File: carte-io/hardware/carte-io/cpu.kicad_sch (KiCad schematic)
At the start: 24 parts, among them J3 FTSH-105-01-L-DV-007, SW1 SW_Push, SW2 SW_Push, U1 STM32U545VETx, X1 ASE-16.000MHZ-LC-T

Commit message: Carte version 1.1 terminée
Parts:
- J3: value FTSH-105-01-L-DV-007 -> FTSH-105-01-L-DH; footprint FTSH-105-01-L-DV-007-K:SAMTEC_FTSH-105-X-X-DV-007-P-X -> FTSH-105-01-L-DH:SAMTEC_FTSH-105-01-L-DH
- R28: value 1K -> 270R
- SW1, SW2: footprint Button_Switch_THT:SW_TH_Tactile_Omron_B3F-10xx -> Button_Switch_SMD:Panasonic_EVQPUJ_EVQPUA
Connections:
- net GEN_PWM1: no longer names the net of U1.67 (PA8)
- net GEN_PWM2: no longer names the net of U1.47 (PB10)
- net INPUT1 renamed IO1
- net INPUT2 renamed IO2
- net INPUT3 renamed IO3
- net INPUT4 renamed IO4
- net OUTPUT1: no longer names the net of U1.42 (PE11)
- net OUTPUT2 renamed ADC_AN1
- net OUTPUT3: no longer names the net of U1.45 (PE14)
- net OUTPUT4: no longer names the net of U1.46 (PE15)
- net SPI_CS: no longer names the net of U1.97 (PE0)
- net SPI_MISO: no longer names the net of U1.31 (PA6)
- net SPI_MOSI: no longer names the net of U1.32 (PA7)
- net SPI_SCK renamed ADC_AN2
- no-connect marks 18 -> 26
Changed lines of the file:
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@@
 	(title_block
 		(title "CPU")
-		(date "2024-10-09")
-		(rev "1.0")
+		(date "2025-02-25")
+		(rev "1.1")
 	)
 	(junction
@@
 	)
 	(no_connect
+		(at 104.14 58.42)
+	)
+	(no_connect
+		(at 149.86 104.14)
+	)
+	(no_connect
+		(at 104.14 86.36)
+	)
+	(no_connect
 		(at 149.86 114.3)
 	)
@@
 	)
 	(no_connect
+		(at 149.86 53.34)
+	)
+	(no_connect
 		(at 149.86 154.94)
 	)
@@
 	)
 	(no_connect
+		(at 149.86 50.8)
+	)
+	(no_connect
 		(at 104.14 60.96)
 	)
 	(no_connect
+		(at 149.86 55.88)
+	)
+	(no_connect
 		(at 149.86 73.66)
 	)
 	(no_connect
+		(at 104.14 96.52)
+	)
+	(no_connect
 		(at 149.86 157.48)
 	)
@@
 	)
 	(no_connect
+		(at 104.14 93.98)
+	)
+	(no_connect
 		(at 104.14 137.16)
 	)
@@
 	(wire
 		(pts
-			(xy 91.44 91.44) (xy 104.14 91.44)
+			(xy 50.8 187.96) (xy 58.42 187.96)
 		)
 		(stroke
@@
 	(wire
 		(pts
-			(xy 50.8 187.96) (xy 58.42 187.96)
+			(xy 91.44 88.9) (xy 104.14 88.9)
 		)
 		(stroke
@@
 	(wire
 		(pts
-			(xy 149.86 104.14) (xy 163.83 104.14)
-		)
-		(stroke
-			(width 0)
-			(type default)
-		)
-	)
-	(wire
-		(pts
 			(xy 91.44 124.46) (xy 104.14 124.46)
 		)
@@
 	(wire
 		(pts
-			(xy 91.44 86.36) (xy 104.14 86.36)
-		)
-		(stroke
-			(width 0)
-			(type default)
-		)
-	)
-	(wire
-		(pts
 			(xy 58.42 187.96) (xy 58.42 189.23)
 		)
@@
 	(wire
 		(pts
-			(xy 91.44 93.98) (xy 104.14 93.98)
+			(xy 91.44 91.44) (xy 104.14 91.44)
 		)
 		(stroke
@@
 	(wire
 		(pts
-			(xy 91.44 88.9) (xy 104.14 88.9)
-		)
-		(stroke
-			(width 0)
-			(type default)
-		)
-	)
-	(wire
-		(pts
 			(xy 25.4 130.81) (xy 25.4 128.27)
 		)
@@
 	(wire
 		(pts
-			(xy 149.86 50.8) (xy 163.83 50.8)
-		)
-		(stroke
-			(width 0)
-			(type default)
-		)
-	)
-	(wire
-		(pts
-			(xy 91.44 96.52) (xy 104.14 96.52)
-		)
-		(stroke
-			(width 0)
-			(type default)
-		)
-	)
-	(wire
-		(pts
 			(xy 76.2 43.18) (xy 90.17 43.18)
 		)
@@
 	(wire
 		(pts
-			(xy 96.52 58.42) (xy 104.14 58.42)
-		)
-		(stroke
-			(width 0)
-			(type default)
-		)
-	)
-	(wire
-		(pts
 			(xy 149.86 71.12) (xy 163.83 71.12)
 		)
@@
 	(wire
 		(pts
-			(xy 149.86 55.88) (xy 163.83 55.88)
-		)
-		(stroke
-			(width 0)
-			(type default)
-		)
-	)
-	(wire
-		(pts
 			(xy 44.45 55.88) (xy 44.45 58.42)
 		)
@@
 	(wire
 		(pts
-			(xy 149.86 53.34) (xy 163.83 53.34)
-		)
-		(stroke
-			(width 0)
-			(type default)
-		)
-	)
-	(wire
-		(pts
 			(xy 90.17 33.02) (xy 100.33 33.02)
 		)
@@
 		)
 	)
-	(hierarchical_label "OUTPUT2"
-		(shape output)
-		(at 91.44 88.9 180)
-		(effects
-			(font
-				(size 1.27 1.27)
-			)
-			(justify right)
-		)
-	)
-	(hierarchical_label "GEN_PWM1"
-		(shape output)
-		(at 163.83 55.88 0)
-		(effects
-			(font
-				(size 1.27 1.27)
-			)
-			(justify left)
-		)
-	)
 	(hierarchical_label "US_PulseStart"
 		(shape output)
@@
 		)
 	)
-	(hierarchical_label "OUTPUT3"
-		(shape output)
-		(at 91.44 93.98 180)
-		(effects
-			(font
-				(size 1.27 1.27)
-			)
-			(justify right)
-		)
-	)
 	(hierarchical_label "COM_USB_RX"
 		(shape input)
@@
 		)
 	)
-	(hierarchical_label "SPI_SCK"
-		(shape output)
-		(at 91.44 91.44 180)
-		(effects
-			(font
-				(size 1.27 1.27)
-			)
-			(justify right)
-		)
-	)
-	(hierarchical_label "SPI_MOSI"
-		(shape output)
-		(at 163.83 53.34 0)
-		(effects
-			(font
-				(size 1.27 1.27)
-			)
-			(justify left)
-		)
-	)
-	(hierarchical_label "OUTPUT1"
-		(shape output)
-		(at 91.44 86.36 180)
+	(hierarchical_label "ADC_AN1"
+		(shape input)
+		(at 91.44 88.9 180)
 		(effects
 			(font
@@
 		)
 	)
-	(hierarchical_label "GEN_PWM2"
-		(shape output)
-		(at 163.83 104.14 0)
-		(effects
-			(font
-				(size 1.27 1.27)
-			)
-			(justify left)
-		)
-	)
 	(hierarchical_label "INT_MAGNETO"
 		(shape input)
@@
 		)
 	)
-	(hierarchical_label "INPUT3"
-		(shape input)
+	(hierarchical_label "IO3"
+		(shape bidirectional)
 		(at 91.44 81.28 180)
 		(effects
@@
 		)
 	)
-	(hierarchical_label "OUTPUT4"
-		(shape output)
-		(at 91.44 96.52 180)
-		(effects
-			(font
-				(size 1.27 1.27)
-			)
-			(justify right)
-		)
-	)
 	(hierarchical_label "ENCODER_2_PHB"
 		(shape input)
@@
 		)
 	)
-	(hierarchical_label "INPUT4"
-		(shape input)
+	(hierarchical_label "IO4"
+		(shape bidirectional)
 		(at 91.44 83.82 180)
 		(effects
@@
 		)
 	)
+	(hierarchical_label "ADC_AN2"
+		(shape input)
+		(at 91.44 91.44 180)
+		(effects
+			(font
+				(size 1.27 1.27)
+			)
+			(justify right)
+		)
+	)
 	(hierarchical_label "COM_USB_TX"
 		(shape output)
@@
 		)
 	)
-	(hierarchical_label "INPUT2"
-		(shape input)
+	(hierarchical_label "IO2"
+		(shape bidirectional)
 		(at 91.44 78.74 180)
 		(effects
@@
 		)
 	)
-	(hierarchical_label "SPI_CS"
-		(shape output)
-		(at 96.52 58.42 180)
-		(effects
-			(font
-				(size 1.27 1.27)
-			)
-			(justify right)
-		)
-	)
 	(hierarchical_label "ADC_VBAT"
 		(shape input)
@@
 		)
 	)
-	(hierarchical_label "INPUT1"
-		(shape input)
+	(hierarchical_label "IO1"
+		(shape bidirectional)
 		(at 91.44 76.2 180)
 		(effects
@@
 		)
 	)
-	(hierarchical_label "SPI_MISO"
-		(shape input)
-		(at 163.83 50.8 0)
-		(effects
-			(font
-				(size 1.27 1.27)
-			)
-			(justify left)
-		)
-	)
 	(symbol
 		(lib_id "power:GND")
@@
 			)
 		)
-		(property "Footprint" "Button_Switch_THT:SW_TH_Tactile_Omron_B3F-10xx"
+		(property "Footprint" "Button_Switch_SMD:Panasonic_EVQPUJ_EVQPUA"
 			(at 243.84 49.53 0)
 			(effects
@@
 			)
 		)
-		(property "Value" "FTSH-105-01-L-DV-007"
+		(property "Value" "FTSH-105-01-L-DH"
 			(at 233.68 121.92 0)
 			(effects
@@
 			)
 		)
-		(property "Footprint" "FTSH-105-01-L-DV-007-K:SAMTEC_FTSH-105-X-X-DV-007-P-X"
+		(property "Footprint" "FTSH-105-01-L-DH:SAMTEC_FTSH-105-01-L-DH"
 			(at 233.68 132.08 0)
 			(effects
@@
 			)
 		)
-		(property "Footprint" "Button_Switch_THT:SW_TH_Tactile_Omron_B3F-10xx"
+		(property "Footprint" "Button_Switch_SMD:Panasonic_EVQPUJ_EVQPUA"
 			(at 226.06 49.53 0)
 			(effects
@@
 			)
 		)
-		(property "Value" "1K"
+		(property "Value" "270R"
 			(at 217.17 38.0999 0)
 			(effects

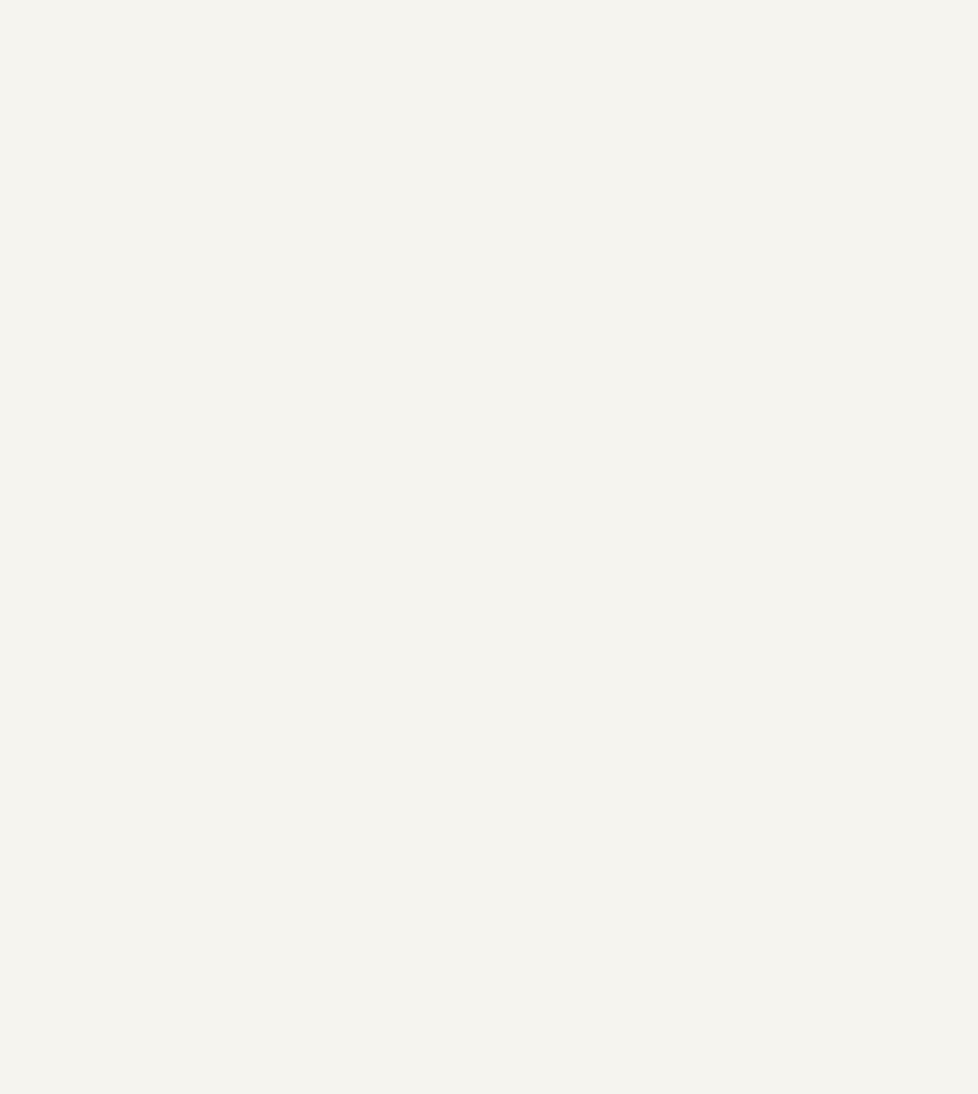
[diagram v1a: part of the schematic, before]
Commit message: WIP ajout du driver uart (marche) et du driver I2C (juste generé par chatgpt, à reprendre et tester)
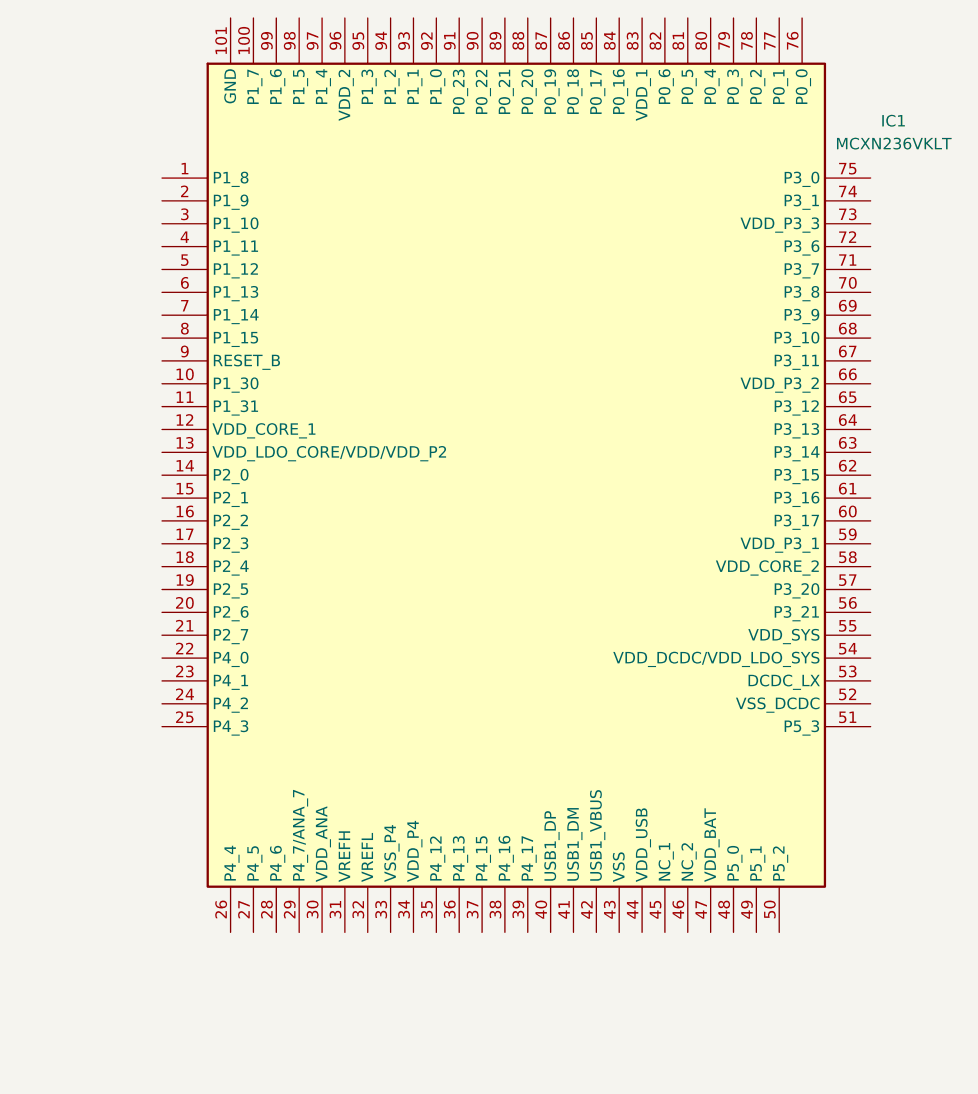
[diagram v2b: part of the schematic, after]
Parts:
- added IC1: MCXN236VKLT, Package_QFP:LQFP-100_14x14mm_P0.5mm, symbol MCXN236VKLT:MCXN236VKLT
